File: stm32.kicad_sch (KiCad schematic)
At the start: 48 parts, among them IC1 LTC3621EMS8E-3.3#PBF, J1 TC2030, J2 USB_C_Receptacle_PowerOnly_6P, SW1 SW_Push, U1 STM32F411CEUx, U2 BMI088, U3 BMP388, U4 W25Q128JVSIQ, U5 TP4056-42-ESOP8, Y1 Crystal_GND24

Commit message: next steps
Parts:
- added D3: SS14, Diode_SMD:D_SMA, symbol Diode:SS14
- added D4: 1N4148WS, Diode_SMD:D_SOD-323, symbol Diode:1N4148WS
- added Q1: DMG2305UX, Custom_Library:DMG2305UX, symbol 2026-04-12_18-39-20:DMG2305UX
- added Q2: FS8205A, FS8205A:SOP65P640X120-8N, symbol 2026-04-12_18-39-20:FS8205A
- added R13: 100k, Resistor_SMD:R_0402_1005Metric, symbol Device:R
- added U6: DW01A, Package_TO_SOT_SMD:SOT-23-6, symbol Battery_Management:DW01A
- Y1: value Crystal_GND24 -> 25MHz
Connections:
- net GND: now also C19.2, Q2.6, Q2.7, R13.2, U6.6 (GND); no longer C19.1
- net VIN_BUCK: now also D3.1 (K), Q1.3 (D)
- net at IC1.6 (INTVCC), IC1.7 (MODE/SYNC): now also C19.1; no longer C19.2
- net +5V renamed VBUS_5V
- net VBUS_5V: now also D3.2 (A), D4.2 (A)
- new net: Q2.2, Q2.3, U6.1 (OD)
- new net: Q2.5, U6.3 (OC)
- new net BAT-: Q2.1, Q2.8, U6.2 (CS)
- new net BAT_OUT: Q1.2 (S)
- new net GATE_LS: D4.1 (K), Q1.1 (G), R13.1
- no-connect marks 4 -> 5
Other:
- moved on the sheet: C19

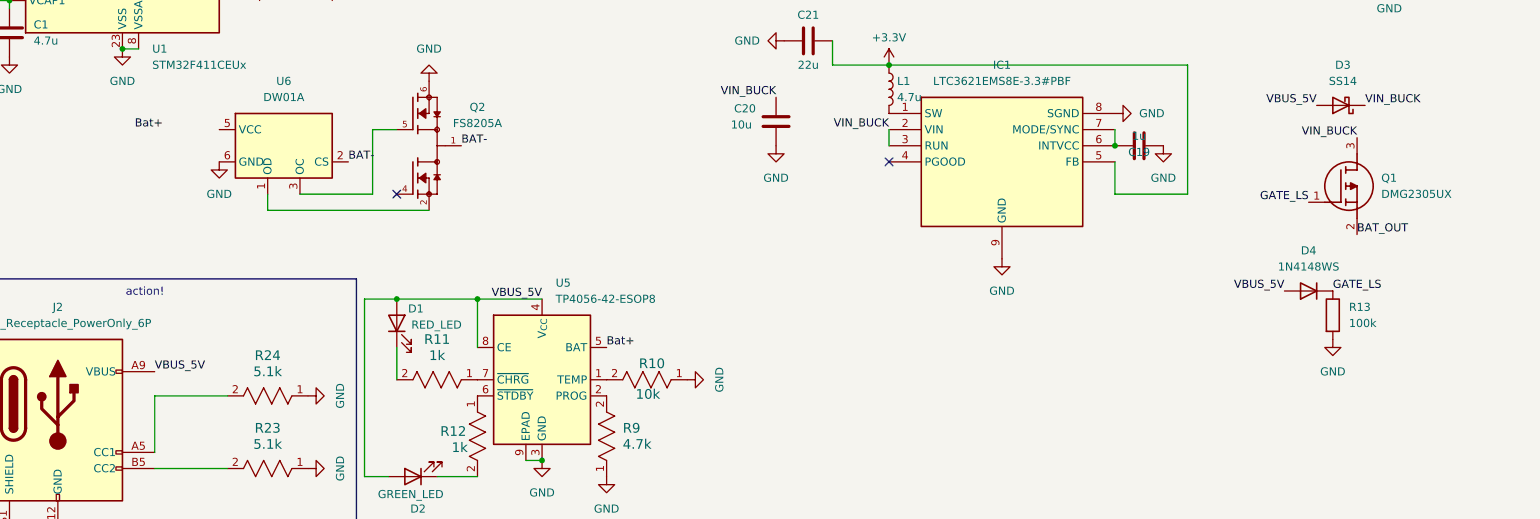
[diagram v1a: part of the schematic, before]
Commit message: Fix DW01A/FS8205A protection wiring and load-share P-FET orientation
- DW01A: VSS->Bat- (cell neg), VM->1k->GND sense, VDD<-100R<-Bat+ with 0.1uF bypass
- Correct gate drive: OD->FS8205 G1, OC->FS8205 G2; remove G1 no-connect
- Float FS8205 common drain (was tied to BAT-)
- Swap load-share P-FET S/D so body diode conducts Bat+->VIN_BUCK
- Merge BAT_OUT into Bat+; rename cell-negative net to Bat-
- Add buck input/output caps; gitignore datasheets and local backup
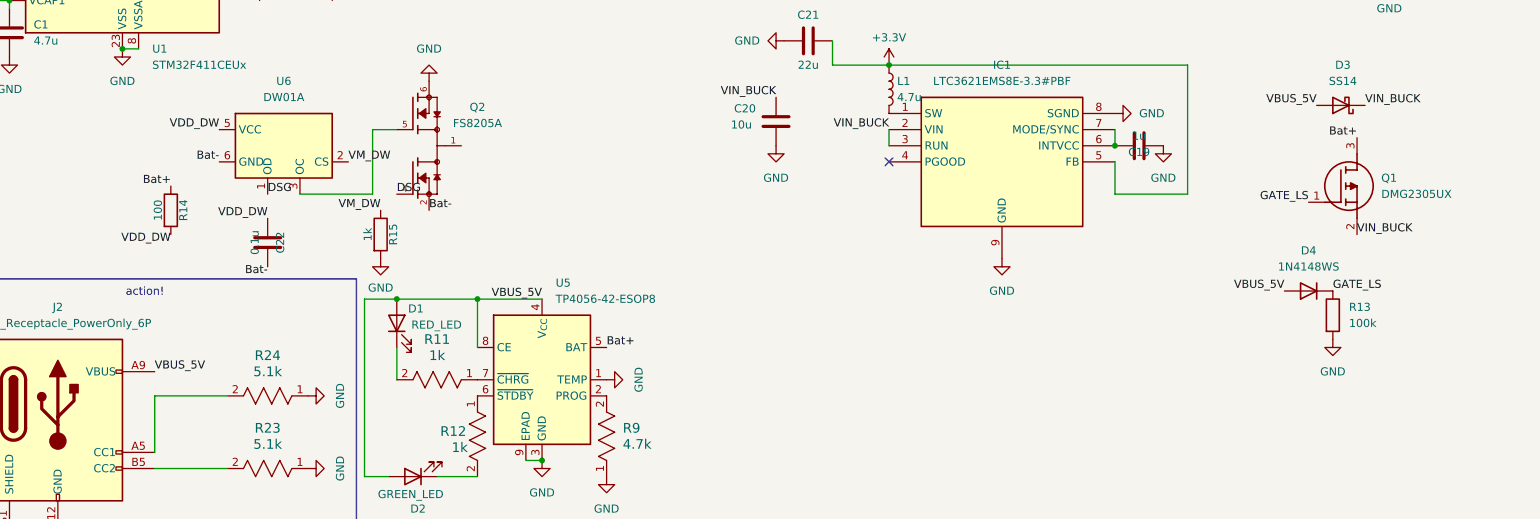
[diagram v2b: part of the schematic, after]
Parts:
- removed R10: 10k, Resistor_SMD:R_0402_1005Metric, symbol 240Library:CF14JT1K00
- added C22: 0.1u, Capacitor_SMD:C_0402_1005Metric, symbol Device:C
- added R14: 100, Resistor_SMD:R_0402_1005Metric, symbol Device:R
- added R15: 1k, Resistor_SMD:R_0402_1005Metric, symbol Device:R
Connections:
- net BAT_OUT is gone; now on net VIN_BUCK: Q1.2 (S)
- net Bat+: now also Q1.3 (D), R14.1
- net GND: now also U5.1 (TEMP), R15.2; no longer U6.6 (GND)
- net VIN_BUCK: no longer Q1.3 (D)
- net Bat-: now reaches Q2.2, Q2.3
- net Bat-: now also U6.6 (GND), C22.2; no longer U6.1 (OD)
- net DSG: now reaches Q2.4
- net DSG: now also U6.1 (OD)
- net VDD_DW: now reaches U6.5 (VCC)
- net VDD_DW: now also C22.1, R14.2
- net BAT-: no longer names the net of Q2.1, Q2.8
- net BAT-: no longer U6.2 (CS)
- new net VM_DW: R15.1, U6.2 (CS)
- no-connect marks 5 -> 4

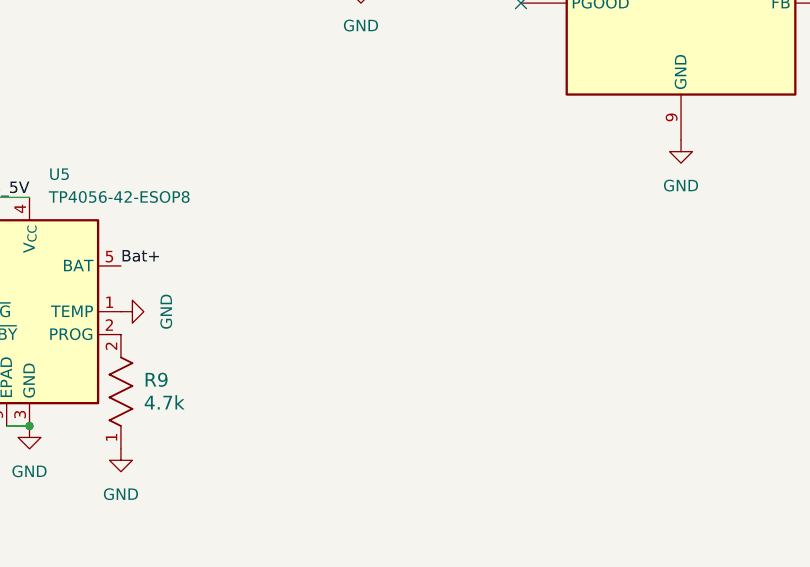
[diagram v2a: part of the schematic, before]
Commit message: added lipo connector
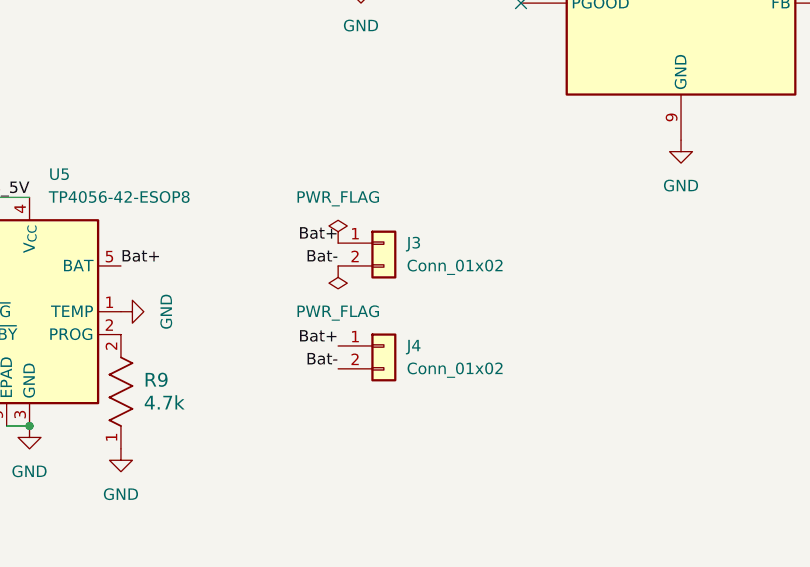
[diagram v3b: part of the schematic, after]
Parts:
- added J3: Conn_01x02, Connector_JST:JST_PH_S2B-PH-SM4-TB_1x02-1MP_P2.00mm_Horizontal, symbol Connector_Generic:Conn_01x02
- added J4: Conn_01x02, Connector_PinHeader_2.54mm:PinHeader_1x02_P2.54mm_Vertical, symbol Connector_Generic:Conn_01x02
- Q2: footprint FS8205A:SOP65P640X120-8N -> Custom_Library:FS8205A
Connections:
- net Bat+: now also J3.1 (Pin_1), J4.1 (Pin_1)
- net Bat-: now also J3.2 (Pin_2), J4.2 (Pin_2)

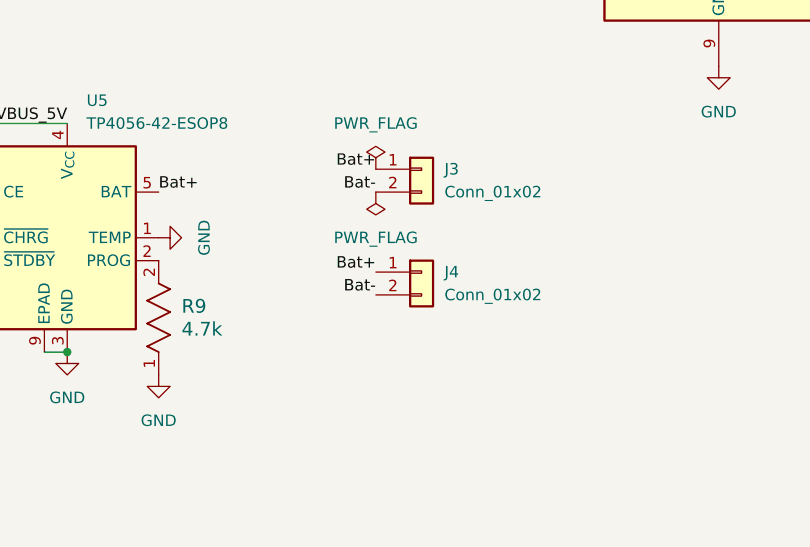
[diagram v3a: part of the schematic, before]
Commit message: Mark J4 battery solder-header as DNP (JST-PH J3 is primary)
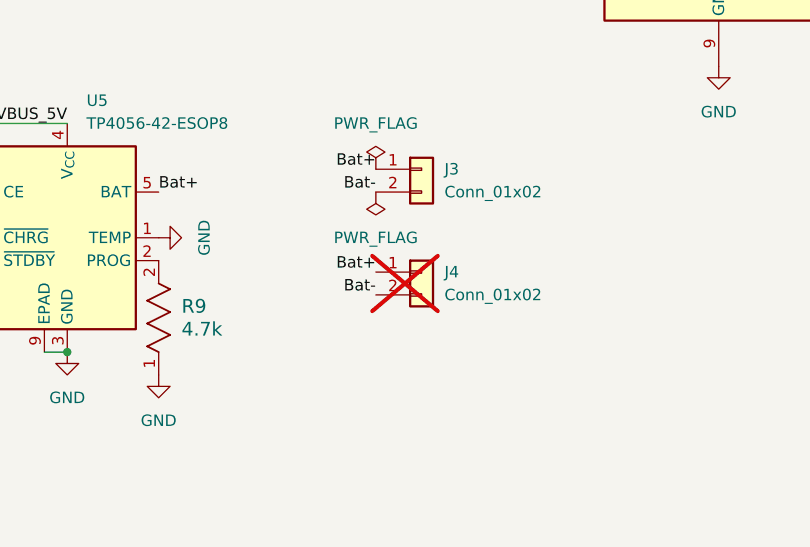
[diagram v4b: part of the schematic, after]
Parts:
- J4: now not fitted
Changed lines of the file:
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@@
 		(in_bom yes)
 		(on_board yes)
-		(dnp no)
+		(dnp yes)
 		(fields_autoplaced yes)
 		(property "Reference" "J4"

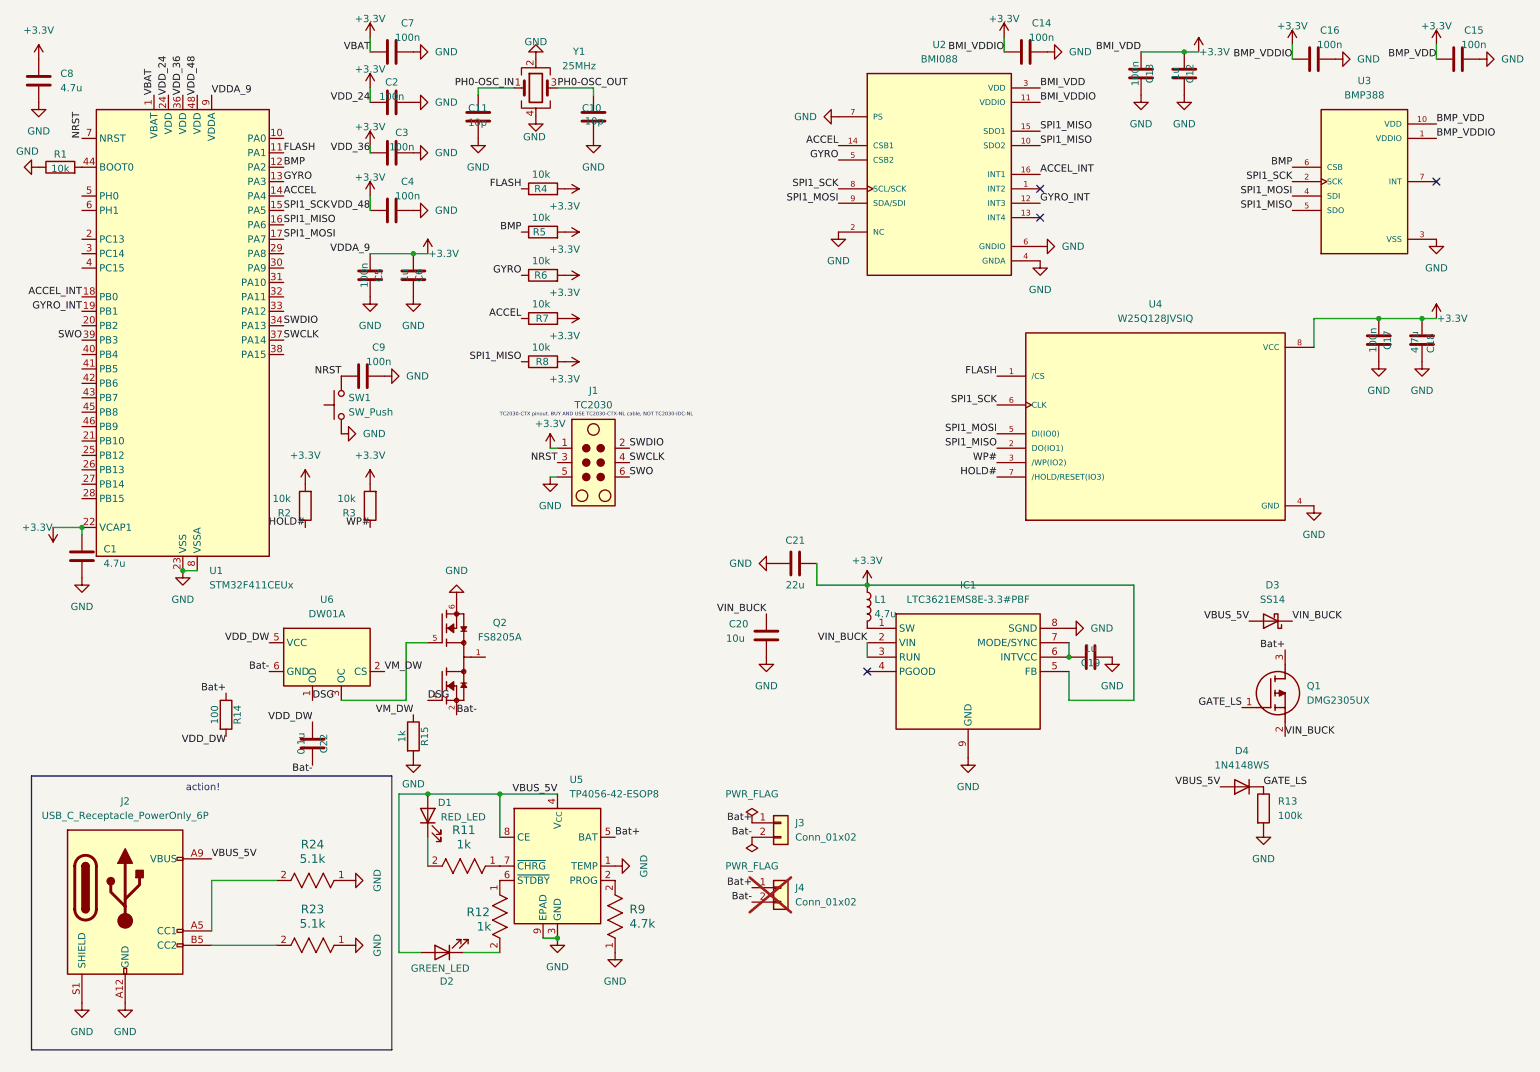
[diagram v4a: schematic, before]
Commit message: Connect HSE crystal to MCU; add LED, logging button, battery sense, UART header
- Wire crystal OSC_IN/OSC_OUT to STM32 PH0/PH1 (was floating)
- Status LED (D5+R16 1k) on PB5, active-high
- Logging button (SW2) on PB4 with 10k pull-up (R17) + 100n debounce (C23)
- Battery sense divider (R18/R19 100k, C24 100n) Bat+ -> PA0 (ADC1_IN0)
- Wire existing UART header J5: PA9 TX, PA10 RX, GND
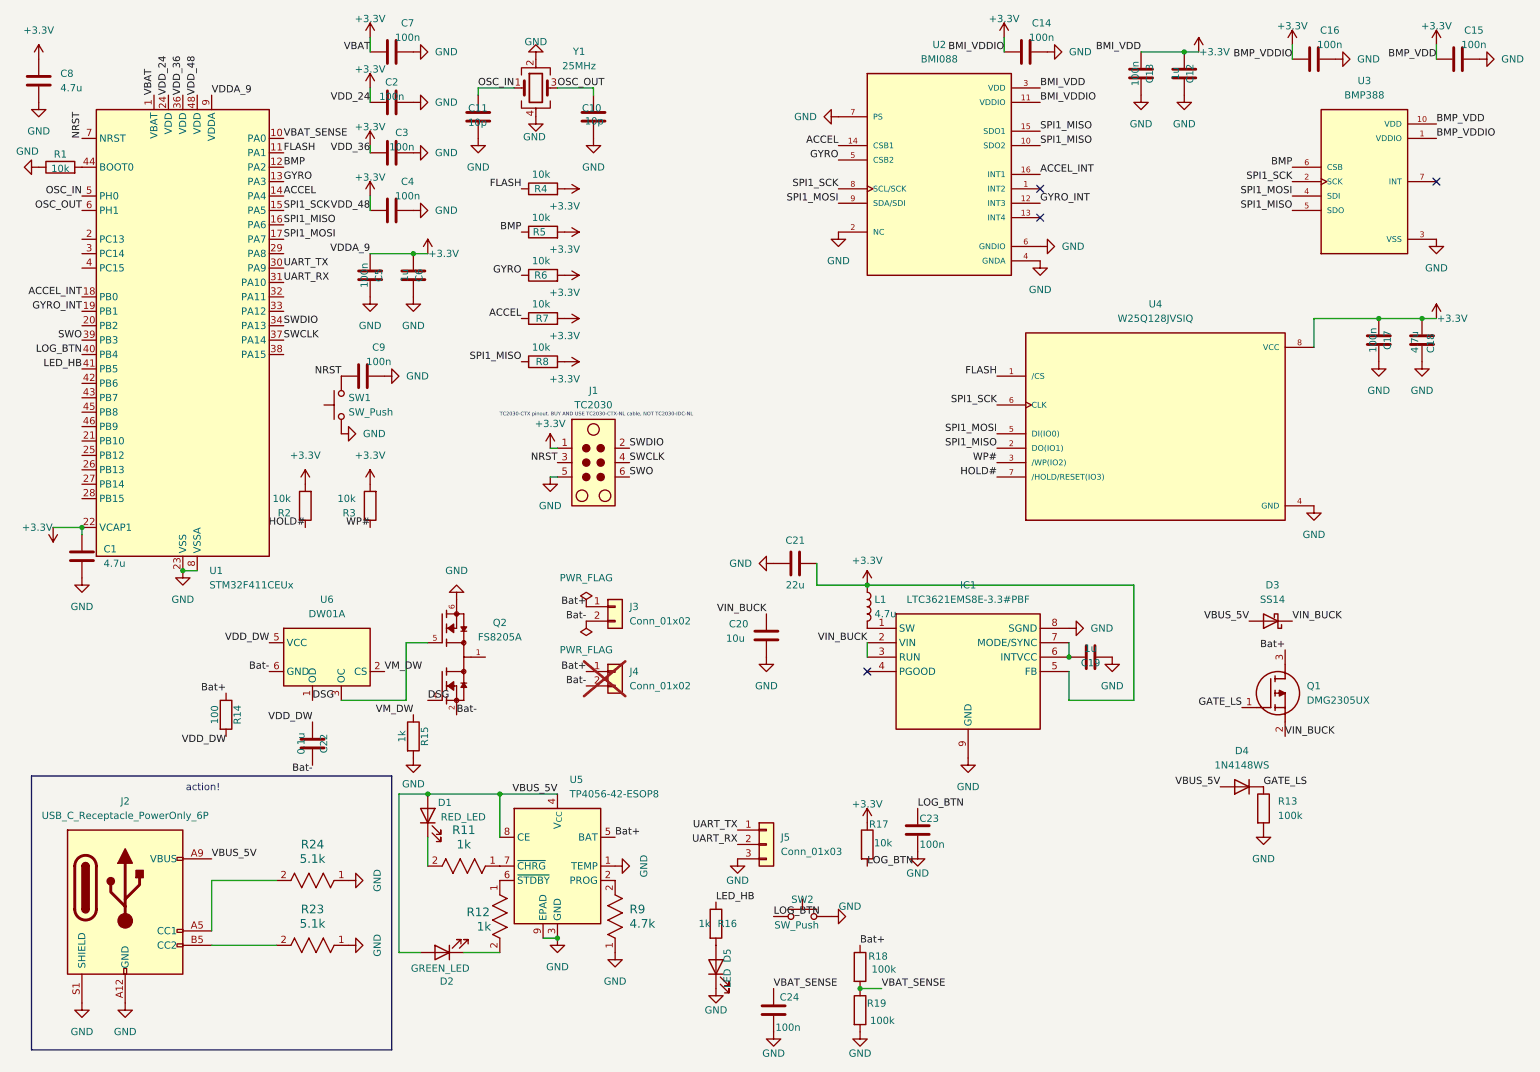
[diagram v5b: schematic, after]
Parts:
- added C23, C24: 100n, Capacitor_SMD:C_0402_1005Metric, symbol Device:C
- added D5: LED, LED_SMD:LED_0603_1608Metric, symbol Device:LED
- added J5: Conn_01x03, symbol Connector_Generic:Conn_01x03
- added R16: 1k, Resistor_SMD:R_0402_1005Metric, symbol Device:R
- added R17: 10k, Resistor_SMD:R_0402_1005Metric, symbol Device:R
- added R18, R19: 100k, Resistor_SMD:R_0402_1005Metric, symbol Device:R
- added SW2: SW_Push, Button_Switch_SMD:SW_SPST_CK_RS282G05A3, symbol Switch:SW_Push
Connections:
- net PH0-OSC_IN is gone; now on net OSC_IN: C11.2, Y1.1
- net PH0-OSC_OUT is gone; now on net OSC_OUT: C10.2, Y1.3
- net +3.3V: now also R17.1
- net Bat+: now also R18.1
- net GND: now also C23.2, C24.2, D5.1 (K), J5.3 (Pin_3), R19.2, SW2.2
- net VBAT_SENSE: now reaches U1.10 (PA0)
- net VBAT_SENSE: now also C24.1, R18.2, R19.1
- net UART_TX: now reaches U1.30 (PA9)
- net UART_TX: now also J5.1 (Pin_1)
- net UART_RX: now reaches U1.31 (PA10)
- net UART_RX: now also J5.2 (Pin_2)
- net LOG_BTN: now reaches U1.40 (PB4)
- net LOG_BTN: now also C23.1, R17.2, SW2.1
- net LED_HB: now reaches U1.41 (PB5)
- net LED_HB: now also R16.1
- net OSC_IN: now reaches U1.5 (PH0)
- net OSC_OUT: now reaches U1.6 (PH1)
- new net: D5.2 (A), R16.2
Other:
- moved on the sheet: J3, J4

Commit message: Add 0R resistors for safety
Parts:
- added R20, R21: 0R, Resistor_SMD:R_0402_1005Metric, symbol Device:R
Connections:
- net SPI1_MOSI: now also R21.2; no longer U1.17 (PA7)
- net SPI1_SCK: now also R20.2; no longer U1.15 (PA5)
- new net MOSI_MCU: R21.1, U1.17 (PA7)
- new net SCK_MCU: R20.1, U1.15 (PA5)
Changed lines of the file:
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@@
 		)
 	)
-	(label "SPI1_MOSI"
+	(label "MOSI_MCU"
 		(at 59.69 52.07 0)
 		(effects
@@
 		)
 	)
+	(label "SCK_MCU"
+		(at 49.69 15.24 0)
+		(effects
+			(font
+				(size 1.27 1.27)
+			)
+			(justify left bottom)
+		)
+	)
+	(label "SPI1_SCK"
+		(at 49.69 22.86 0)
+		(effects
+			(font
+				(size 1.27 1.27)
+			)
+			(justify left top)
+		)
+	)
+	(label "MOSI_MCU"
+		(at 59.69 15.24 0)
+		(effects
+			(font
+				(size 1.27 1.27)
+			)
+			(justify left bottom)
+		)
+	)
+	(label "SPI1_MOSI"
+		(at 59.69 22.86 0)
+		(effects
+			(font
+				(size 1.27 1.27)
+			)
+			(justify left top)
+		)
+	)
 	(label "GATE_LS"
 		(at 232.41 148.59 0)
@@
 		)
 	)
-	(label "SPI1_SCK"
+	(label "SCK_MCU"
 		(at 59.69 46.99 0)
 		(effects
@@
 					(unit 1)
 				)
+			)
+		)
+	)
+	(symbol
+		(lib_id "Device:R")
+		(at 49.69 19.05 0)
+		(unit 1)
+		(exclude_from_sim no)
+		(in_bom yes)
+		(on_board yes)
+		(dnp no)
+		(property "Reference" "R20"
+			(at 51.69 19.05 0)
+			(effects
+				(font
+					(size 1.27 1.27)
+				)
+			)
+		)
+		(property "Value" "0R"
+			(at 47.69 19.05 0)
+			(effects
+				(font
+					(size 1.27 1.27)
+				)
+			)
+		)
+		(property "Footprint" "Resistor_SMD:R_0402_1005Metric"
+			(at 49.69 19.05 90)
+			(effects
+				(font
+					(size 1.27 1.27)
+				)
+				(hide yes)
+			)
+		)
+		(property "Datasheet" "~"
+			(at 49.69 19.05 0)
+			(effects
+				(font
+					(size 1.27 1.27)
+				)
+				(hide yes)
+			)
+		)
+		(property "Description" "Resistor"
+			(at 49.69 19.05 0)
+			(effects
+				(font
+					(size 1.27 1.27)
+				)
+				(hide yes)
+			)
+		)
+		(pin "1"
+		)
+		(pin "2"
+		)
+		(instances
+			(project ""
+				(path "/807257e6-524f-404b-b91f-049b9c2bdd5b"
+					(reference "R20")
+					(unit 1)
+				)
+			)
+		)
+	)
+	(symbol
+		(lib_id "Device:R")
+		(at 59.69 19.05 0)
+		(unit 1)
+		(exclude_from_sim no)
+		(in_bom yes)
+		(on_board yes)
+		(dnp no)
+		(property "Reference" "R21"
+			(at 61.69 19.05 0)
+			(effects
+				(font
+					(size 1.27 1.27)
+				)
+			)
+		)
+		(property "Value" "0R"
+			(at 57.69 19.05 0)
+			(effects
+				(font
+					(size 1.27 1.27)
+				)
+			)
+		)
+		(property "Footprint" "Resistor_SMD:R_0402_1005Metric"
+			(at 59.69 19.05 90)
+			(effects
+				(font
+					(size 1.27 1.27)
+				)
+				(hide yes)
+			)
+		)
+		(property "Datasheet" "~"
+			(at 59.69 19.05 0)
+			(effects
+				(font
+					(size 1.27 1.27)
+				)
+				(hide yes)
+			)
+		)
+		(property "Description" "Resistor"
+			(at 59.69 19.05 0)
+			(effects
+				(font
+					(size 1.27 1.27)
+				)
+				(hide yes)
+			)
+		)
+		(pin "1"
+		)
+		(pin "2"
+		)
+		(instances
+			(project ""
+				(path "/807257e6-524f-404b-b91f-049b9c2bdd5b"
+					(reference "R21")
+					(unit 1)
+				)
